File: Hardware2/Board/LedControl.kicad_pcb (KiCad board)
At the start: 2 copper layers, 69 x 35 mm, 71 parts, among them J1 CONN_01X02, J2 CONN_01X03, J3 CONN_01X03, P1 USB_OTG, P10 CONN_01X01, P11 Micro_SD, P12 CONN_01X01, P13 CONN_01X01, P14 CONN_01X01, P15 CONN_01X03, P16 CONN_01X24, P17 CONN_01X02, P18 CONN_01X02, P19 CONN_01X02, P2 CONN_01X01, P20 CONN_01X03, P21 CONN_01X01, P22 CONN_01X01, P23 CONN_01X01, P24 CONN_01X01, P25 CONN_01X02, P26 CONN_01X02, P27 CONN_01X01, P28 CONN_01X01, P29 CONN_01X02, P3 CONN_01X01, P30 CONN_01X02, P31 CONN_01X05, P32 CONN_01X05, P4 CONN_01X01, P5 CONN_01X01, P6 CONN_01X01, P7 CONN_01X01, P8 CONN_01X01, P9 CONN_01X01, SW1 ROTARY_ENCODER_SWITCH, SW2 ROTARY_ENCODER_SWITCH, U1 STM32L151CCTx, U2 SP3078, U3 SP485CN, U4 TPS82130, U5 LP2985IM5-3.3, U6 TPS82130, U7 SP3485CN, U8 TPS82130, X1 CRYSTAL_SMD, X2 IQXO/7X

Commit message: Finished routing main board
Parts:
- removed P32: CONN_01X05, LedControl:LED_Strip
- removed X2: IQXO/7X, LedControl:Oscillator_5x3.2mm
- added D2: SS 12L, Diodes_SMD:D_1206, F.Cu at (74.6, 117.0)
- added D3: SS 12L, Diodes_SMD:D_1206, F.Cu at (81.5, 117.0)
- added J4: J, LedControl:Jumper, F.Cu at (72.4, 117.0)
- added J5: J, LedControl:Jumper, F.Cu at (83.7, 117.0)
- added J6: J, LedControl:Jumper, B.Cu at (74.1, 109.0)
- added R12: 523k, Resistors_SMD:R_0603, F.Cu at (91.1, 110.2)
- added R13: 100k, Resistors_SMD:R_0603, F.Cu at (92.7, 110.2)
- added R14: 523k, Resistors_SMD:R_0603, F.Cu at (119.7, 92.8)
- added R15: 100k, Resistors_SMD:R_0603, F.Cu at (119.7, 90.2)
- added R16: 523k, Resistors_SMD:R_0603, F.Cu at (104.4, 95.6)
- added R17: 100k, Resistors_SMD:R_0603, F.Cu at (103.2, 97.5)
- added U9: TPS82130, LedControl:TPS82130, F.Cu at (103.7, 90.3)
- J1: value CONN_01X02 -> J; moved to B.Cu
- J2: value CONN_01X03 -> J
- J3: value CONN_01X03 -> CONN_01X02; footprint LedControl:Jumper3 -> LedControl:Jumper; moved to B.Cu
- P1: footprint Connect:USB_Mini-B -> LedControl:Micro_USB
- P10, P14, P2, P21, P22, P23, P27, P3, P4, P6, P7, P9: value CONN_01X01 -> TP; moved to B.Cu
- P11: value Micro_SD -> 2059-302; footprint LedControl:MicroSD -> LedControl:WAGO_2059-302
- P12: value CONN_01X01 -> DISPLAY; footprint LedControl:Pad -> LedControl:Connector_Flat_24_Pitch0.50mm
- P13: value CONN_01X01 -> TP
- P15: value CONN_01X03 -> CONN_01X01; footprint Pin_Headers:Pin_Header_Straight_1x03 -> LedControl:Pad; moved to B.Cu
- P16: value CONN_01X24 -> 2059-302; footprint LedControl:Connector_Flat_24_Pitch0.50mm -> LedControl:WAGO_2059-302
- P17: value CONN_01X02 -> 2059-302
- P18, P19: value CONN_01X02 -> CONN_01X03; footprint LedControl:WAGO_2059-302 -> Pin_Headers:Pin_Header_Straight_1x03
- P20: value CONN_01X03 -> TP; footprint Pin_Headers:Pin_Header_Straight_1x03 -> LedControl:Pad; moved to B.Cu
- P24, P28: value CONN_01X01 -> 2060-452; footprint LedControl:Pad -> LedControl:WAGO_2060-452
- P25: value CONN_01X02 -> 2060-452
- P26: value CONN_01X02 -> TP; footprint LedControl:WAGO_2060-452 -> LedControl:Pad; moved to B.Cu
- P29: value CONN_01X02 -> 2059-302; footprint LedControl:WAGO_2060-452 -> LedControl:WAGO_2059-302
- P30: value CONN_01X02 -> LED_Strip; footprint LedControl:WAGO_2059-302 -> LedControl:LED_Strip
- P5: value CONN_01X01 -> 2059-302; footprint LedControl:Pad -> LedControl:WAGO_2059-302
- P8: value CONN_01X01 -> Micro_SD; footprint LedControl:Pad -> LedControl:Micro_SD
- R10, R6, R8: value 523k -> 120R; footprint Resistors_SMD:R_0603 -> Resistors_SMD:R_1206
- R2: value 470R -> 120R; footprint Resistors_SMD:R_0603 -> Resistors_SMD:R_1206
- R3: value 1M2 -> 523k
- R4, R9: value 100k -> 120R; footprint Resistors_SMD:R_0603 -> Resistors_SMD:R_1206
- R5: value 100k -> 523k
- SW1, SW2: value ROTARY_ENCODER_SWITCH -> PEC12R-4215F-S0024
- U1: value STM32L151CCTx -> STM32L433CCUx; footprint Housings_QFP:LQFP-48_7x7mm_Pitch0.5mm -> Housings_DFN_QFN:QFN-48-1EP_7x7mm_Pitch0.5mm
- U2: value SP3078 -> SP485CN
- U4, U8: value TPS82130 -> SP485CN; footprint LedControl:TPS82130 -> Housings_SOIC:SOIC-8_3.9x4.9mm_Pitch1.27mm
- U5: value LP2985IM5-3.3 -> TPS82130; footprint TO_SOT_Packages_SMD:SOT-23-5 -> LedControl:TPS82130
- U6: value TPS82130 -> LP2985IM5-3.3; footprint LedControl:TPS82130 -> TO_SOT_Packages_SMD:SOT-23-5
- U7: value SP3485CN -> TPS82130; footprint Housings_SOIC:SOIC-8_3.9x4.9mm_Pitch1.27mm -> LedControl:TPS82130
- X1: value CRYSTAL_SMD -> IQXO/7X; footprint LedControl:CSTCE_16 -> LedControl:Oscillator_5x3.2mm; moved to B.Cu
- moved U6 84.5 mm to (87.3, 117.0), turned to 270 degrees
- moved R11 63.8 mm to (84.8, 122.0)
- moved P28 61.6 mm to (128.0, 90.0), turned to 180 degrees
- moved P31 58.4 mm to (98.6, 96.5)
- moved C10 57.6 mm to (116.5, 95.1), turned to 90 degrees
- moved P23 52.4 mm to (89.0, 120.2)
- moved R2 52.1 mm to (129.5, 110.5), turned to 180 degrees
- moved P24 51.4 mm to (72.1, 107.0), turned to 270 degrees
- moved P19 51.3 mm to (77.0, 132.5)
- moved R8 47.2 mm to (82.5, 133.0), turned to 180 degrees
- moved C9 47.0 mm to (117.5, 87.7), turned to 0 degrees
- moved U7 43.2 mm to (116.8, 91.1)
- moved P11 42.4 mm to (126.0, 105.0), turned to 270 degrees
- moved P8 42.1 mm to (94.5, 133.0), turned to 0 degrees
- moved P18 40.7 mm to (91.3, 104.5)
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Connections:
- C1 pad 1: +3V3 -> +5V
- D1 pad 1: Net-(D1-Pad1) -> GND
- J2 pad 1: GND -> +3V3
- J2 pad 3: +3V3 -> +5V
- P11 pad 1: Net-(P11-Pad1) -> Net-(J3-Pad1)
- P12 pad 1: Net-(P12-Pad1) -> GND
- P15 pad 1: GND -> Net-(P15-Pad1)
- P16 pad 1: GND -> Net-(P16-Pad1)
- P16 pad 2: GND -> Net-(P16-Pad2)
- P17 pad 2: Net-(J2-Pad2) -> Net-(P17-Pad2)
- P19 pad 1: Net-(P19-Pad1) -> GND
- P20 pad 1: GND -> +5V
- P21 pad 1: +5V -> +3V3
- P22 pad 1: +3V3 -> +5V
- P23 pad 1: +5V -> +3V3
- P24 pad 1: +3V3 -> GND
- P25 pad 2: VCC -> Net-(D3-Pad2)
- P28 pad 1: GND -> Net-(C10-Pad2)
- P29 pad 1: Net-(C10-Pad2) -> Net-(P29-Pad1)
- P29 pad 2: Net-(C9-Pad1) -> Net-(P29-Pad2)
- P30 pad 1: Net-(P30-Pad1) -> Net-(C10-Pad2)
- P31 pad 1: Net-(C10-Pad2) -> Net-(C11-Pad2)
- P31 pad 3: Net-(C10-Pad1) -> Net-(C12-Pad1)
- P31 pad 4: Net-(C10-Pad2) -> Net-(C11-Pad2)
- P31 pad 5: Net-(C9-Pad1) -> Net-(C11-Pad1)
- P5 pad 1: Net-(P5-Pad1) -> GND
- R10 pad 1: Net-(C12-Pad1) -> Net-(P18-Pad2)
- R10 pad 2: Net-(R10-Pad2) -> Net-(P17-Pad1)
- R11 pad 1: Net-(R10-Pad2) -> GND
- R11 pad 2: Net-(C11-Pad2) -> Net-(R11-Pad2)
- R2 pad 1: Net-(D1-Pad1) -> Net-(J3-Pad2)
- R2 pad 2: GND -> Net-(P11-Pad2)
- R3 pad 1: GND -> Net-(R3-Pad1)
- R3 pad 2: Net-(P16-Pad21) -> Net-(P12-Pad21)
- R4 pad 1: GND -> Net-(P16-Pad1)
- R4 pad 2: Net-(P16-Pad9) -> Net-(R4-Pad2)
- R5 pad 2: Net-(R5-Pad2) -> Net-(R3-Pad1)
- R6 pad 1: +5V -> Net-(P16-Pad2)
- R7 pad 1: Net-(R6-Pad2) -> GND
- R7 pad 2: GND -> Net-(P12-Pad9)
- R8 pad 1: Net-(C10-Pad1) -> Net-(R8-Pad1)
- R8 pad 2: Net-(R8-Pad2) -> Net-(D1-Pad2)
- R9 pad 1: Net-(R8-Pad2) -> Net-(R9-Pad1)
- R9 pad 2: Net-(C10-Pad2) -> Net-(P17-Pad2)
- SW1 pad 4: +3V3 -> Net-(R11-Pad2)
- SW1 pad 5: Net-(R5-Pad2) -> +3V3
- SW2 pad 4: +3V3 -> Net-(SW2-Pad4)
- SW2 pad 5: Net-(SW2-Pad5) -> +3V3
- U1 pad 10: Net-(SW2-Pad1) -> Net-(P8-Pad9)
- U1 pad 11: Net-(SW2-Pad3) -> Net-(U1-Pad11)
- U1 pad 12: Net-(P7-Pad1) -> Net-(U1-Pad12)
- U1 pad 13: Net-(P8-Pad1) -> Net-(U1-Pad13)
- U1 pad 14: Net-(P9-Pad1) -> Net-(P8-Pad2)
- U1 pad 15: Net-(P10-Pad1) -> Net-(P8-Pad5)
- U1 pad 16: Net-(P12-Pad1) -> Net-(P8-Pad7)
- U1 pad 17: Net-(P13-Pad1) -> Net-(P8-Pad3)
- U1 pad 18: Net-(SW2-Pad5) -> Net-(SW2-Pad4)
- U1 pad 19: Net-(P6-Pad1) -> Net-(U1-Pad19)
- U1 pad 2: Net-(P3-Pad1) -> Net-(P4-Pad1)
- U1 pad 20: Net-(P16-Pad9) -> Net-(P12-Pad9)
- U1 pad 25: Net-(P16-Pad8) -> Net-(P12-Pad8)
- U1 pad 26: Net-(P16-Pad13) -> Net-(P12-Pad13)
- U1 pad 27: Net-(U1-Pad27) -> Net-(P15-Pad1)
- U1 pad 28: Net-(P16-Pad14) -> Net-(P12-Pad14)
- U1 pad 29: Net-(P14-Pad1) -> Net-(SW1-Pad3)
- U1 pad 3: Net-(P4-Pad1) -> Net-(P6-Pad1)
- U1 pad 30: Net-(P15-Pad3) -> Net-(SW1-Pad1)
- U1 pad 31: Net-(P15-Pad2) -> Net-(P12-Pad10)
- U1 pad 34: Net-(P16-Pad10) -> Net-(P13-Pad1)
- U1 pad 37: Net-(D1-Pad2) -> Net-(P14-Pad1)
- U1 pad 38: Net-(P11-Pad2) -> Net-(SW2-Pad3)
- U1 pad 39: Net-(P11-Pad5) -> Net-(SW2-Pad1)
- U1 pad 4: Net-(P5-Pad1) -> Net-(P7-Pad1)
- U1 pad 40: Net-(P11-Pad7) -> Net-(P9-Pad1)
- U1 pad 41: Net-(P11-Pad3) -> Net-(P10-Pad1)
- U1 pad 42: Net-(SW1-Pad1) -> Net-(P19-Pad3)
- U1 pad 43: Net-(SW1-Pad3) -> Net-(P19-Pad2)
- U1 pad 44: Net-(R5-Pad2) -> Net-(R11-Pad2)
- U1 pad 45: Net-(R5-Pad2) -> Net-(R11-Pad2)
- U1 pad 46: Net-(P11-Pad9) -> Net-(R8-Pad1)
- U1 pad 6: Net-(U1-Pad6) -> Net-(P2-Pad1)
- U1 pad 7: Net-(P2-Pad1) -> Net-(P3-Pad1)
- U2 pad 2: +3V3 -> Net-(U1-Pad19)
- U2 pad 3: Net-(U1-Pad27) -> Net-(U1-Pad19)
- U2 pad 6: Net-(P18-Pad2) -> Net-(J3-Pad1)
- U2 pad 7: Net-(P17-Pad1) -> Net-(P11-Pad2)
- U2 pad 8: +3V3 -> +5V
- U3 pad 1: Net-(U3-Pad1) -> Net-(U1-Pad13)
- U3 pad 2: +5V -> Net-(U1-Pad11)
- U3 pad 3: +5V -> Net-(U1-Pad11)
- U3 pad 4: Net-(P15-Pad3) -> Net-(U1-Pad12)
- U3 pad 6: Net-(P19-Pad2) -> Net-(R4-Pad2)
- U3 pad 7: Net-(P19-Pad1) -> Net-(R6-Pad2)
- U4 pad 1: VCC -> Net-(U4-Pad1)
- U4 pad 2: VCC -> +5V
- U4 pad 3: GND -> +5V
- U4 pad 4: +5V -> Net-(P19-Pad3)
- U4 pad 5: +5V -> GND
- U4 pad 6: Net-(R6-Pad2) -> Net-(R9-Pad1)
- U4 pad 7: Net-(U4-Pad7) -> Net-(P18-Pad2)
- U4 pad 8: Net-(U4-Pad8) -> +5V
- U5 pad 1: +5V -> VCC
- U5 pad 2: GND -> VCC
- U5 pad 3: +5V -> GND
- U5 pad 4: Net-(U5-Pad4) -> +5V
- U5 pad 5: +3V3 -> +5V
- U6 pad 1: Net-(C9-Pad1) -> +5V
- U6 pad 2: Net-(C9-Pad1) -> GND
- U6 pad 3: Net-(C10-Pad2) -> +5V
- U6 pad 4: Net-(C10-Pad1) -> Net-(U6-Pad4)
- U6 pad 5: Net-(C10-Pad1) -> +3V3
- U7 pad 1: Net-(P31-Pad2) -> Net-(C9-Pad1)
- U7 pad 2: Net-(C10-Pad2) -> Net-(C9-Pad1)
- U7 pad 4: Net-(C10-Pad2) -> Net-(C10-Pad1)
- U7 pad 5: Net-(C10-Pad2) -> Net-(C10-Pad1)
- U7 pad 6: Net-(P30-Pad1) -> Net-(R14-Pad2)
- U7 pad 7: Net-(P30-Pad2) -> Net-(U7-Pad7)
- U7 pad 8: Net-(C10-Pad1) -> Net-(U7-Pad8)
- U8 pad 1: Net-(C11-Pad1) -> Net-(P30-Pad2)
- U8 pad 2: Net-(C11-Pad1) -> Net-(C10-Pad2)
- U8 pad 3: Net-(C11-Pad2) -> Net-(C10-Pad2)
- U8 pad 4: Net-(C12-Pad1) -> Net-(C10-Pad2)
- U8 pad 5: Net-(C12-Pad1) -> Net-(C10-Pad2)
- U8 pad 6: Net-(R10-Pad2) -> Net-(P29-Pad1)
- U8 pad 7: Net-(U8-Pad7) -> Net-(P29-Pad2)
- U8 pad 8: Net-(U8-Pad8) -> Net-(C10-Pad1)
- X1 pad 1: Net-(U1-Pad5) -> +3V3
- X1 pad 2: Net-(U1-Pad6) -> GND
- X1 pad 3: GND -> Net-(U1-Pad5)
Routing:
- net +3V3: track 0.00 -> 138.5 mm, vias 0 -> 5
- net +5V: track 0.00 -> 131.0 mm, vias 0 -> 6
- net Net-(P19-Pad3): track 0.00 -> 70.5 mm, vias 0 -> 2
- net Net-(R11-Pad2): track 0.00 -> 66.5 mm, vias 0 -> 1
- net Net-(C10-Pad2): track 0.00 -> 65.7 mm, vias 0 -> 3
- net GND: track 0.00 -> 47.8 mm, vias 0 -> 4
- net Net-(P19-Pad2): track 0.00 -> 40.2 mm, vias 0 -> 1
- net Net-(SW1-Pad3): track 0.00 -> 39.8 mm
- net VCC: track 0.00 -> 39.3 mm, vias 0 -> 2
- net Net-(P18-Pad2): track 0.00 -> 37.6 mm, vias 0 -> 1
- net Net-(SW1-Pad1): track 0.00 -> 35.7 mm
- net Net-(SW2-Pad1): track 0.00 -> 34.1 mm
- net Net-(U1-Pad22): track 0.00 -> 33.8 mm, vias 0 -> 2
- net Net-(R8-Pad1): track 0.00 -> 32.1 mm, vias 0 -> 2
- net Net-(P12-Pad9): track 0.00 -> 31.9 mm, vias 0 -> 2
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- added copper zone on B.Cu, net GND
- added copper zone on F.Cu, net GND
- added copper zone on B.Cu, net Net-(D2-Pad2)
- added copper zone on B.Cu, net Net-(D3-Pad2)
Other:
- outline, holes or cut-outs redrawn

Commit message: routing nearly finished
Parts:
- removed R5: 523k, Resistors_SMD:R_0603
- added C13: 100n, Capacitors_SMD:C_0603, F.Cu at (74.3, 115.5)
- added C14: 100n, Capacitors_SMD:C_0603, F.Cu at (83.5, 115.5)
- added P32: TP, LedControl:Pad, B.Cu at (101.5, 120.5)
- added P33: TP, LedControl:Pad, B.Cu at (99.9, 120.5)
- added R18: 52k3, Resistors_SMD:R_0603, F.Cu at (72.1, 116.6)
- added R19: 52k3, Resistors_SMD:R_0603, F.Cu at (81.3, 116.6)
- added R20: 10k, Resistors_SMD:R_0603, F.Cu at (74.2, 117.1)
- added R21: 10k, Resistors_SMD:R_0603, F.Cu at (83.4, 117.1)
- C11, C6, C9: value 10u/25V/X7R -> 10u
- P30: footprint LedControl:LED_Strip -> LedControl:LED_Strip_Start
- P31: value CONN_01X05 -> LED_Strip
- R11, R13, R15, R17: value 100k -> 10k
- R12, R14, R16: value 523k -> 52k3
- R3: value 523k -> 1M2
- R7: value 100k -> 52k3
- moved R8 49.0 mm to (131.5, 133.1), turned to 0 degrees
- moved D1 48.9 mm to (131.4, 130.4), turned to 0 degrees
- moved P23 34.0 mm to (122.7, 124.0)
- moved P4 18.7 mm to (94.2, 131.6)
- moved P10 18.2 mm to (98.2, 115.0)
- moved P9 16.5 mm to (100.8, 115.0)
- moved P6 15.7 mm to (99.1, 133.0)
- moved P13 12.2 mm to (113.0, 123.4)
- moved P31 8.53 mm to (107.0, 98.0)
- moved C11 7.53 mm to (110.2, 87.8)
- moved R17 7.40 mm to (110.6, 97.5)
- moved P14 6.54 mm to (94.2, 128.5)
- moved C12 6.50 mm to (110.0, 93.7), turned to 180 degrees
- moved R16 6.20 mm to (110.6, 95.7)
- moved U9 6.17 mm to (109.8, 90.8)
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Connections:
- C11 pad 2: Net-(C11-Pad2) -> Net-(C10-Pad2)
- C12 pad 1: Net-(C12-Pad1) -> Net-(C10-Pad1)
- C12 pad 2: Net-(C11-Pad2) -> Net-(C10-Pad2)
- C9 pad 1: Net-(C9-Pad1) -> Net-(C11-Pad1)
- P12 pad 14: Net-(P12-Pad14) -> Net-(P10-Pad1)
- P28 pad 2: Net-(C9-Pad1) -> Net-(C11-Pad1)
- P30 pad 5: Net-(C9-Pad1) -> Net-(C11-Pad1)
- P31 pad 1: Net-(C11-Pad2) -> Net-(C10-Pad2)
- P31 pad 2: Net-(P31-Pad2) -> Net-(P30-Pad2)
- P31 pad 3: Net-(C12-Pad1) -> Net-(C10-Pad1)
- P31 pad 4: Net-(C11-Pad2) -> Net-(C10-Pad2)
- P9 pad 1: Net-(P9-Pad1) -> Net-(P12-Pad13)
- R16 pad 1: Net-(C12-Pad1) -> Net-(C10-Pad1)
- R17 pad 2: Net-(C11-Pad2) -> Net-(C10-Pad2)
- R3 pad 1: Net-(R3-Pad1) -> GND
- SW1 pad 4: Net-(R11-Pad2) -> +3V3
- SW1 pad 5: +3V3 -> Net-(R11-Pad2)
- SW2 pad 4: Net-(SW2-Pad4) -> +3V3
- SW2 pad 5: +3V3 -> Net-(SW2-Pad5)
- U1 pad 10: Net-(P8-Pad9) -> Net-(SW2-Pad3)
- U1 pad 11: Net-(U1-Pad11) -> Net-(SW2-Pad1)
- U1 pad 14: Net-(P8-Pad2) -> Net-(P13-Pad1)
- U1 pad 17: Net-(P8-Pad3) -> /Power/U1
- U1 pad 18: Net-(SW2-Pad4) -> /Power/U2
- U1 pad 2: Net-(P4-Pad1) -> Net-(U1-Pad2)
- U1 pad 27: Net-(P15-Pad1) -> Net-(P8-Pad9)
- U1 pad 28: Net-(P12-Pad14) -> Net-(P10-Pad1)
- U1 pad 3: Net-(P6-Pad1) -> Net-(R11-Pad2)
- U1 pad 34: Net-(P13-Pad1) -> Net-(P14-Pad1)
- U1 pad 37: Net-(P14-Pad1) -> Net-(P15-Pad1)
- U1 pad 38: Net-(SW2-Pad3) -> Net-(P8-Pad2)
- U1 pad 39: Net-(SW2-Pad1) -> Net-(P4-Pad1)
- U1 pad 4: Net-(P7-Pad1) -> Net-(SW2-Pad5)
- U1 pad 40: Net-(P9-Pad1) -> Net-(P6-Pad1)
- U1 pad 41: Net-(P10-Pad1) -> Net-(P8-Pad3)
- U1 pad 45: Net-(R11-Pad2) -> Net-(P7-Pad1)
- U3 pad 2: Net-(U1-Pad11) -> Net-(U1-Pad2)
- U3 pad 3: Net-(U1-Pad11) -> Net-(U1-Pad2)
- U7 pad 1: Net-(C9-Pad1) -> Net-(C11-Pad1)
- U7 pad 2: Net-(C9-Pad1) -> Net-(C11-Pad1)
- U9 pad 3: Net-(C11-Pad2) -> Net-(C10-Pad2)
- U9 pad 4: Net-(C12-Pad1) -> Net-(C10-Pad1)
- U9 pad 5: Net-(C12-Pad1) -> Net-(C10-Pad1)
- U9 pad 9: Net-(C11-Pad2) -> Net-(C10-Pad2)
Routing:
- net Net-(C10-Pad2): track 65.7 -> 136.5 mm, vias 3 -> 12
- net Net-(R11-Pad2): track 66.5 -> 133.6 mm
- net /Power/U1: track 0.00 -> 46.0 mm, vias 0 -> 2
- net Net-(C11-Pad1): track 0.00 -> 44.8 mm, vias 0 -> 3
- net /Power/U2: track 0.00 -> 35.7 mm, vias 0 -> 2
- net Net-(C10-Pad1): track 15.9 -> 43.2 mm, vias 1 -> 4
- net Net-(C9-Pad1): track 25.2 -> 0.00 mm, vias 2 -> 0
- net +3V3: track 138.5 -> 156.7 mm
- net Net-(U1-Pad2): track 0.00 -> 17.7 mm, vias 0 -> 2
- net GND: track 47.8 -> 64.7 mm
- net Net-(U1-Pad11): track 14.1 -> 0.00 mm
- net Net-(P10-Pad1): track 4.35 -> 16.8 mm
- net Net-(P8-Pad9): track 31.0 -> 18.9 mm
- net Net-(SW2-Pad4): track 11.8 -> 0.00 mm
- net Net-(P12-Pad14): track 11.6 -> 0.00 mm
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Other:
- board text added: "16V GND 16V GND"
- board text added: "B A B A B A LED1 LED2 485"
- board text added: "GND"
- board text added: "PWR"

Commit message: Update to KiCad 5.0.1, add debug connector
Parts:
- removed J1: J, LedControl:Jumper
- added D4: D, Diode_SMD:D_1206_3216Metric, F.Cu at (129.6, 130.0)
- C1, C13, C14, C2, C3, C4: footprint Capacitors_SMD:C_0603 -> Capacitor_SMD:C_0603_1608Metric
- C10, C12, C7, C8: footprint Capacitors_SMD:C_0805 -> Capacitor_SMD:C_0805_2012Metric
- C11, C5, C6, C9: footprint Capacitors_SMD:C_1206 -> Capacitor_SMD:C_1206_3216Metric
- D1: footprint LEDs:LED_0805 -> LED_SMD:LED_0805_2012Metric
- D2, D3: footprint Diodes_SMD:D_1206 -> Diode_SMD:D_1206_3216Metric
- J2: value J -> Jumper
- J3: value CONN_01X02 -> Jumper
- P14: value TP -> Conn_01x03; footprint LedControl:Pad -> Connector_PinHeader_2.00mm:PinHeader_1x03_P2.00mm_Vertical
- P15: value CONN_01X01 -> TP
- P18, P19: footprint Pin_Headers:Pin_Header_Straight_1x03 -> Connector_PinHeader_2.54mm:PinHeader_1x03_P2.54mm_Vertical
- R1, R11, R12, R13, R14, R15, R16, R17, R18, R19, R20, R21, R3, R7: footprint Resistors_SMD:R_0603 -> Resistor_SMD:R_0603_1608Metric
- R10, R2, R4, R6, R8, R9: footprint Resistors_SMD:R_1206 -> Resistor_SMD:R_1206_3216Metric
- U1: footprint Housings_DFN_QFN:QFN-48-1EP_7x7mm_Pitch0.5mm -> Package_DFN_QFN:QFN-48-1EP_7x7mm_P0.5mm_EP5.6x5.6mm
- U2, U3, U4, U8: footprint Housings_SOIC:SOIC-8_3.9x4.9mm_Pitch1.27mm -> Package_SO:SOIC-8_3.9x4.9mm_P1.27mm
- U6: footprint TO_SOT_Packages_SMD:SOT-23-5 -> Package_TO_SOT_SMD:SOT-23-5
- moved P14 14.7 mm to (80.0, 132.4), turned to 270 degrees
- moved P15 10.1 mm to (91.8, 132.9)
- moved P12 6.00 mm to (100.0, 113.0), turned to 180 degrees
- moved P19 1.60 mm to (70.4, 132.5)
- moved D1 1.56 mm to (132.9, 130.2), turned to 270 degrees
- moved C4 0.42 mm to (103.8, 131.6), turned to 270 degrees
- moved R8 0.35 mm to (131.5, 133.4)
- moved R15 0.15 mm to (119.7, 90.0)
- moved R14 0.15 mm to (119.7, 92.7)
- moved C7 0.05 mm to (87.8, 113.9)
- moved P6 0.05 mm to (99.1, 132.9)
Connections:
- net /Power/U1 renamed U1
- net /Power/U2 renamed U2
- net Net-(P1-Pad2) renamed USB_DM
- net Net-(P1-Pad3) renamed USB_DP
- net Net-(P10-Pad1) renamed DISP_MOSI
- net Net-(P12-Pad10) renamed DISP_D_C#
- net Net-(P12-Pad13) renamed DISP_SCK
- net Net-(P12-Pad8) renamed DISP_NSS
- net Net-(P12-Pad9) renamed DISP_RES#
- net Net-(P19-Pad2) renamed TTY_RX
- net Net-(P19-Pad3) renamed STRIP1_TTY_TX
- net Net-(P8-Pad2) renamed SD_NSS
- net Net-(P8-Pad3) renamed SD_MOSI
- net Net-(P8-Pad5) renamed SD_SCK
- net Net-(P8-Pad7) renamed SD_MISO
- net Net-(P8-Pad9) renamed SD_DET
- net Net-(R8-Pad1) renamed DEBUG_LED
- net Net-(U1-Pad12) renamed STRIP2_TX
- net Net-(U1-Pad13) renamed STRIP2_RX
- net Net-(U1-Pad19) renamed RS485_DE
- net Net-(U1-Pad2) renamed STRIP2_DE
- net Net-(U1-Pad21) renamed RS485_TX
- net Net-(U1-Pad22) renamed RS485_RX
- P14 pad 1: Net-(P14-Pad1) -> SWDCLK
- P15 pad 1: Net-(P15-Pad1) -> GND
- R11 pad 2: Net-(R11-Pad2) -> ENC1_SW
- U1 pad 10: Net-(SW2-Pad3) -> ENC2_CH1
- U1 pad 11: Net-(SW2-Pad1) -> ENC2_CH2
- U1 pad 29: Net-(SW1-Pad3) -> ENC1_CH1
- U1 pad 3: Net-(R11-Pad2) -> ENC1_SW
- U1 pad 30: Net-(SW1-Pad1) -> ENC1_CH2
- U1 pad 34: Net-(P14-Pad1) -> SWDIO
- U1 pad 37: Net-(P15-Pad1) -> SWDCLK
- U1 pad 4: Net-(SW2-Pad5) -> ENC2_SW
- U1 pad 44: Net-(R11-Pad2) -> ENC1_SW
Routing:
- net Net-(R11-Pad2): track 133.6 -> 0.00 mm, vias 1 -> 0
- net ENC1_SW: track 0.00 -> 133.5 mm, vias 0 -> 1
- net ENC1_CH1: track 0.00 -> 39.8 mm
- net Net-(SW1-Pad3): track 39.8 -> 0.00 mm
- net Net-(SW1-Pad1): track 35.7 -> 0.00 mm
- net ENC1_CH2: track 0.00 -> 35.7 mm
- net SWDCLK: track 0.00 -> 31.4 mm, vias 0 -> 2
- net SWDIO: track 0.00 -> 28.7 mm, vias 0 -> 1
- net Net-(SW2-Pad1): track 23.7 -> 0.00 mm
- net ENC2_CH2: track 0.00 -> 23.7 mm
- net Net-(SW2-Pad3): track 20.4 -> 0.00 mm
- net ENC2_CH1: track 0.00 -> 20.3 mm
- net Net-(SW2-Pad5): track 11.5 -> 0.00 mm
- net ENC2_SW: track 0.00 -> 11.5 mm
- net Net-(P14-Pad1): track 11.5 -> 0.00 mm, vias 1 -> 0
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
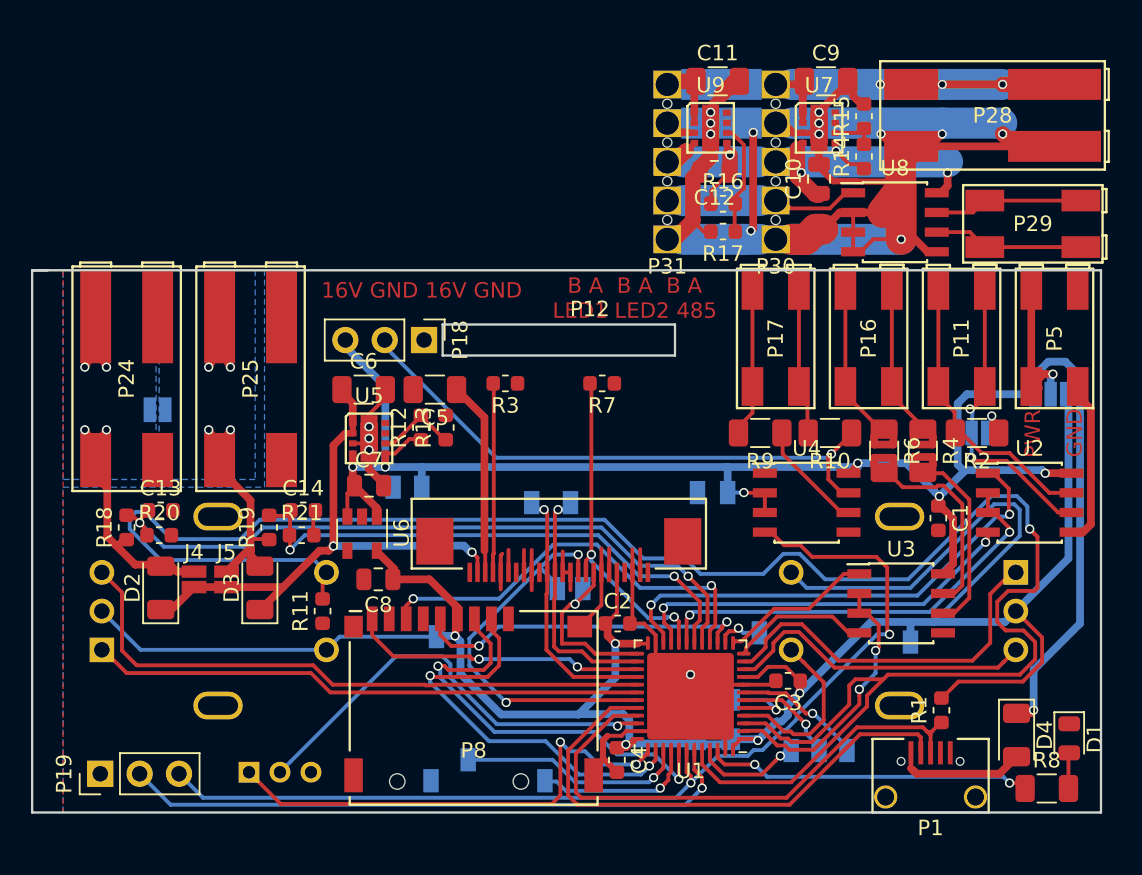
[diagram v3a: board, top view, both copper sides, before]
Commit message: Board is ready for production, needs last review
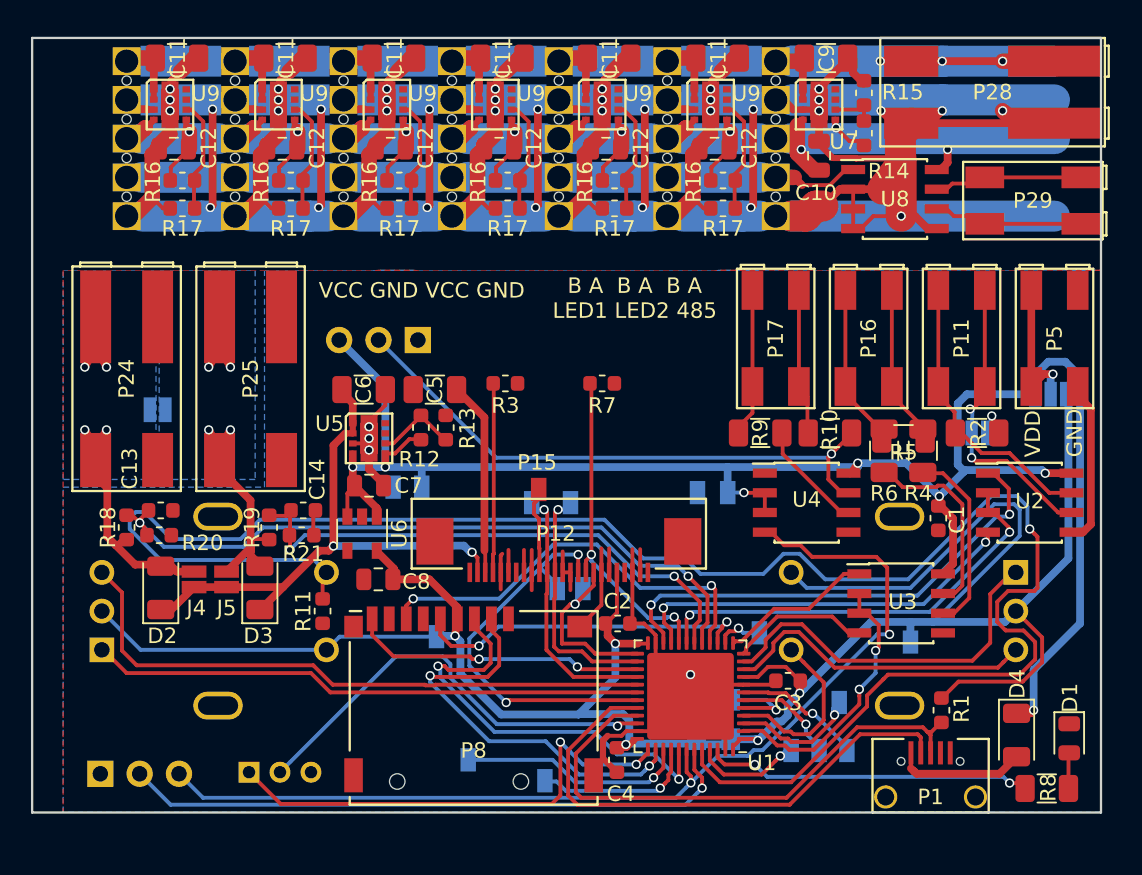
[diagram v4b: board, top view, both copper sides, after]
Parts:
- removed the C12 at (110.0, 93.7)
- added C11: 10u, Capacitor_SMD:C_1206_3216Metric, F.Cu at (75.3, 86.3)
- added C11: 10u, Capacitor_SMD:C_1206_3216Metric, F.Cu at (82.3, 86.3)
- added C11: 10u, Capacitor_SMD:C_1206_3216Metric, F.Cu at (89.3, 86.3)
- added C11: 10u, Capacitor_SMD:C_1206_3216Metric, F.Cu at (96.3, 86.3)
- added C11: 10u, Capacitor_SMD:C_1206_3216Metric, F.Cu at (103.2, 86.3)
- added C12: 22u, Capacitor_SMD:C_0805_2012Metric, F.Cu at (75.2, 92.2)
- added C12: 22u, Capacitor_SMD:C_0805_2012Metric, F.Cu at (82.2, 92.2)
- added C12: 22u, Capacitor_SMD:C_0805_2012Metric, F.Cu at (89.2, 92.2)
- added C12: 22u, Capacitor_SMD:C_0805_2012Metric, F.Cu at (96.2, 92.2)
- added C12: 22u, Capacitor_SMD:C_0805_2012Metric, F.Cu at (103.0, 92.2)
- added C12: 22u, Capacitor_SMD:C_0805_2012Metric, F.Cu at (110.0, 92.2)
- added DIVIDER1: Divider_22mm, LedControl:Divider_22mm, F.Cu at (78.0, 99.0)
- added DIVIDER2: Divider_21mm, LedControl:Divider_21mm, F.Cu at (100.5, 99.0)
- added DIVIDER3: Divider_22mm, LedControl:Divider_22mm, F.Cu at (123.0, 99.0)
- added P31: LED_Strip, LedControl:LED_Strip, F.Cu at (72.1, 96.5)
- added P31: LED_Strip, LedControl:LED_Strip, F.Cu at (79.1, 96.5)
- added P31: LED_Strip, LedControl:LED_Strip, F.Cu at (86.1, 96.5)
- added P31: LED_Strip, LedControl:LED_Strip, F.Cu at (93.1, 96.5)
- added P31: LED_Strip, LedControl:LED_Strip, F.Cu at (100.0, 96.5)
- added P34: TP, LedControl:Pad, B.Cu at (118.1, 127.9)
- added R16: 52k3, Resistor_SMD:R_0603_1608Metric, F.Cu at (75.7, 94.2)
- added R16: 52k3, Resistor_SMD:R_0603_1608Metric, F.Cu at (82.7, 94.2)
- added R16: 52k3, Resistor_SMD:R_0603_1608Metric, F.Cu at (89.7, 94.2)
- added R16: 52k3, Resistor_SMD:R_0603_1608Metric, F.Cu at (96.7, 94.2)
- added R16: 52k3, Resistor_SMD:R_0603_1608Metric, F.Cu at (103.6, 94.2)
- added R17: 10k, Resistor_SMD:R_0603_1608Metric, F.Cu at (75.7, 96.0)
- added R17: 10k, Resistor_SMD:R_0603_1608Metric, F.Cu at (82.7, 96.0)
- added R17: 10k, Resistor_SMD:R_0603_1608Metric, F.Cu at (89.7, 96.0)
- added R17: 10k, Resistor_SMD:R_0603_1608Metric, F.Cu at (96.7, 96.0)
- added R17: 10k, Resistor_SMD:R_0603_1608Metric, F.Cu at (103.6, 96.0)
- added R5: 120R, Resistor_SMD:R_1206_3216Metric, F.Cu at (122.2, 110.9)
- added SLOT: Slot_15x2mm, LedControl:Slot_15x2mm, F.Cu at (100.0, 104.5)
- added U9: TPS82130, LedControl:TPS82130, F.Cu at (74.9, 89.3)
- added U9: TPS82130, LedControl:TPS82130, F.Cu at (81.9, 89.3)
- added U9: TPS82130, LedControl:TPS82130, F.Cu at (88.9, 89.3)
- added U9: TPS82130, LedControl:TPS82130, F.Cu at (95.9, 89.3)
- added U9: TPS82130, LedControl:TPS82130, F.Cu at (102.8, 89.3)
- P15: moved to F.Cu
- P18, P19: moved to B.Cu
- moved P15 20.0 mm to (98.7, 114.2), turned to 270 degrees
- moved C10 1.50 mm to (116.8, 92.6)
- moved C11 1.50 mm to (110.2, 86.3)
- moved C9 1.50 mm to (117.2, 86.3)
- moved P28 1.50 mm to (128.0, 88.5)
- moved P29 1.50 mm to (130.0, 95.5)
- moved P30 1.50 mm to (114.0, 96.5)
- moved P31 1.50 mm to (107.0, 96.5)
- moved R14 1.50 mm to (119.7, 91.2)
- moved R15 1.50 mm to (119.7, 88.5)
- moved R16 1.50 mm to (110.6, 94.2)
- moved R17 1.50 mm to (110.6, 96.0)
- moved U7 1.50 mm to (116.8, 89.3)
- moved U8 1.50 mm to (121.7, 95.4)
- moved U9 1.50 mm to (109.8, 89.3)
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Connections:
- P15 pad 1: GND -> Net-(P12-Pad15)
- U1 pad 3: ENC1_SW -> Net-(P34-Pad1)
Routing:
- net (no net): track 0.00 -> 434.8 mm, vias 0 -> 30
- net Net-(C10-Pad2): track 136.5 -> 149.8 mm
- net ENC1_SW: track 133.5 -> 121.5 mm
- net Net-(P34-Pad1): track 0.00 -> 8.45 mm, vias 0 -> 1
- net Net-(R16-Pad2): track 7.27 -> 14.5 mm
- net Net-(C10-Pad1): track 43.2 -> 49.3 mm
- net Net-(P12-Pad15): track 0.00 -> 5.62 mm
- net Net-(P16-Pad2): track 14.5 -> 9.85 mm
- net Net-(P16-Pad1): track 13.1 -> 9.63 mm
- net Net-(C11-Pad1): track 44.8 -> 48.2 mm
- net Net-(R6-Pad2): track 15.9 -> 12.7 mm
- net Net-(R4-Pad2): track 15.3 -> 12.2 mm
- net RS485_RX: track 34.2 -> 31.8 mm
- net GND: track 64.9 -> 62.9 mm
- net Net-(P30-Pad2): track 12.6 -> 13.6 mm
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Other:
- board size 69 x 35 mm -> 69 x 50 mm
- board text added: "3V3"
- board text added: "5V"
- board text added: "RS485 TERM"
- board text added: "VCC GND VCC GND"
- board text added: "VDD"
- board text removed: "16V GND 16V GND"
- board text removed: "PWR"
